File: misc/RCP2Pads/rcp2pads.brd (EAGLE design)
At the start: 16.2 x 24.1 mm, 57 parts

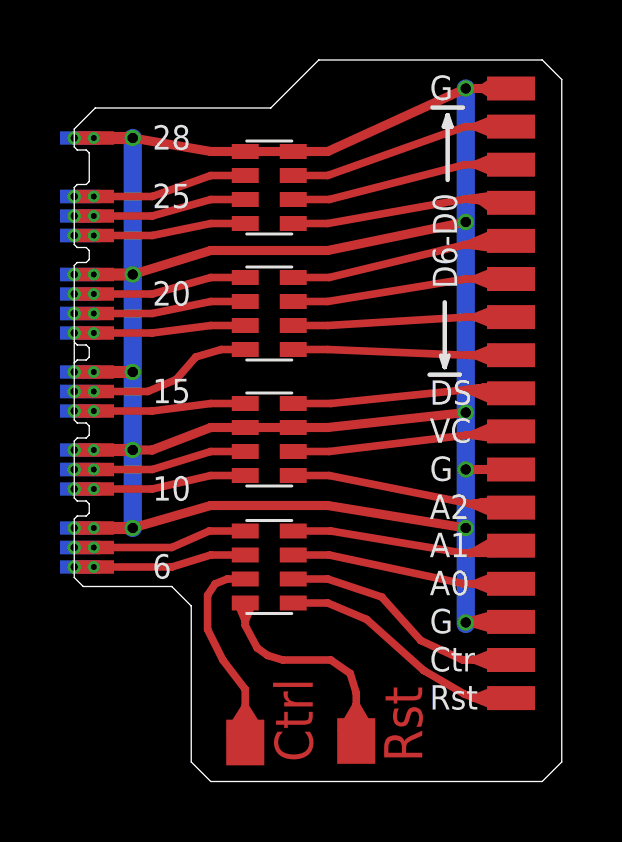
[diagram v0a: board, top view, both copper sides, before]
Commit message: upload new design for RCP2Pads
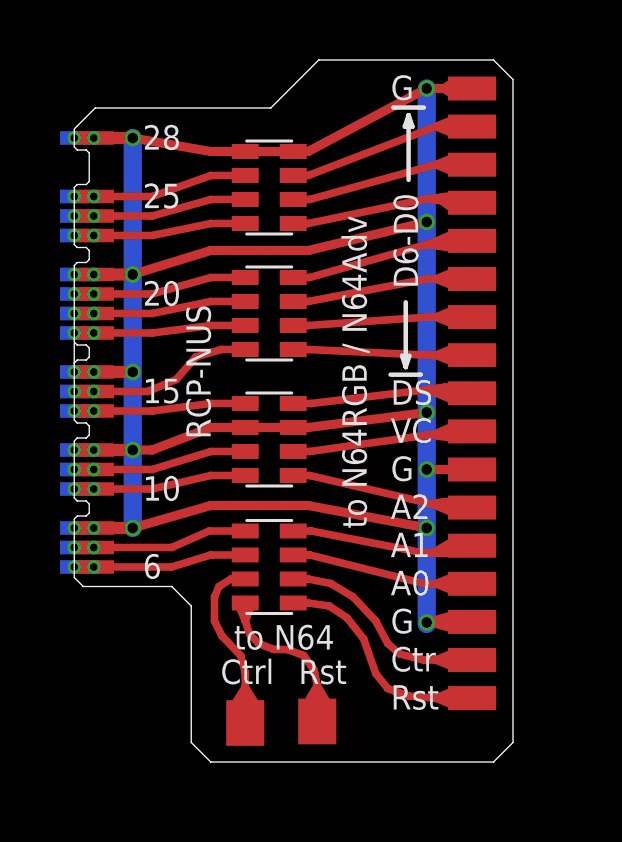
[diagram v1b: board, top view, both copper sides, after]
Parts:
- moved E$6 1.45 mm to (8.10, -8.40)
- moved E$20 1.30 mm to (13.3, 11.4)
- moved E$21 1.30 mm to (13.3, 12.7)
- moved E$36 1.30 mm to (13.3, 10.2)
- moved E$39 1.30 mm to (13.3, 8.89)
- moved E$48 1.30 mm to (13.3, 7.62)
- moved E$49 1.30 mm to (13.3, 6.35)
- moved E$50 1.30 mm to (13.3, 5.08)
- moved E$51 1.30 mm to (13.3, 3.81)
- moved E$53 1.30 mm to (13.3, 2.54)
- moved E$54 1.30 mm to (13.3, 1.27)
- moved E$55 1.30 mm to (13.3, 0.00)
- moved E$56 1.30 mm to (13.3, -1.27)
- moved E$57 1.30 mm to (13.3, -2.54)
- moved E$58 1.30 mm to (13.3, -3.81)
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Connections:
- new net S$2: E$12.P$1, E$29.P$1
- net GND: no longer E$12.P$1, E$29.P$1
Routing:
- net GND: track 92.5 -> 86.1 mm, vias 21 -> 18
- net RST: track 10.5 -> 8.66 mm
- net S$2: track 0.00 -> 1.30 mm, vias 0 -> 3
- net D6.1: track 9.63 -> 8.33 mm
- net D5.1: track 9.14 -> 7.85 mm
- net #DSYNC.1: track 10.0 -> 8.74 mm
- net VCLK.1: track 9.86 -> 8.57 mm
- net D4.1: track 9.20 -> 7.91 mm
- net SDATA.1: track 9.94 -> 8.65 mm
- net D1.1: track 10.4 -> 9.13 mm
- net D2.1: track 10.8 -> 9.47 mm
- net LRCLK.1: track 10.2 -> 8.88 mm
- net SCLK.1: track 9.24 -> 7.95 mm
- net D3.1: track 9.83 -> 8.55 mm
- net D0.1: track 10.6 -> 9.29 mm
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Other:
- board size 16.2 x 24.1 mm -> 14.6 x 23.4 mm
- board text added: "RCP-NUS"
- board text added: "borti4938 __/)__/)_"
- board text added: "to N64"
- board text added: "to N64RGB / N64Adv"

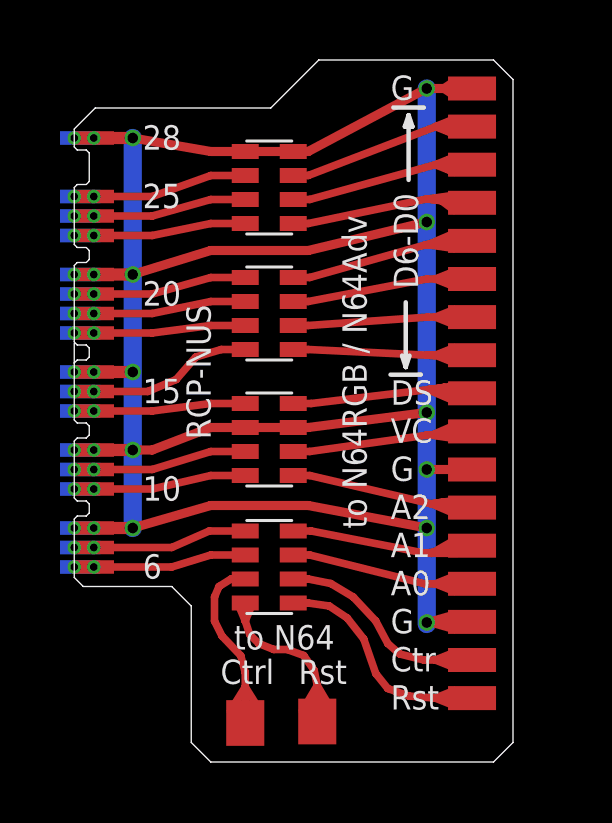
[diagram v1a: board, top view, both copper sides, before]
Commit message: update on adapter flex to include a vlck buffer
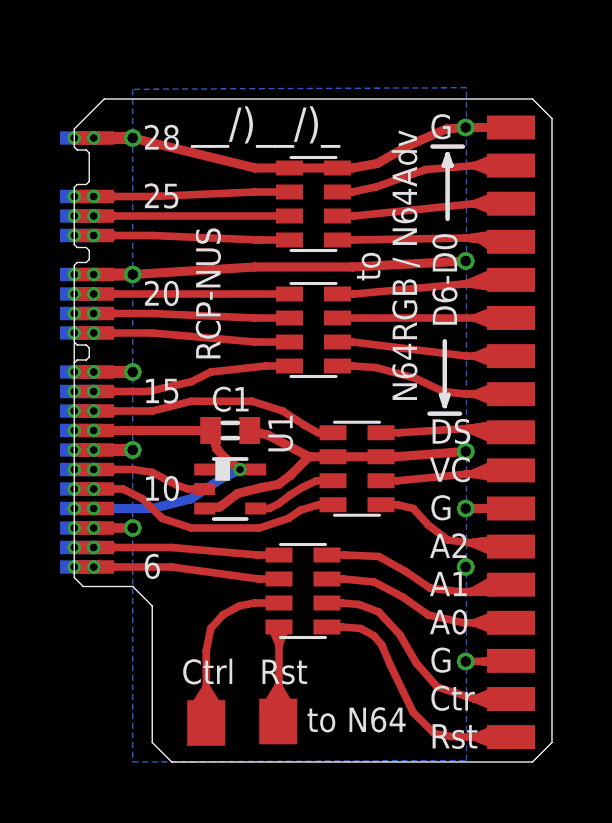
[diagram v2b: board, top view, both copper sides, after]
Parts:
- removed E$1, E$3, E$4, E$5: (no value), resistor-net:CTS742C083
- added C1: (no value), rcl:C0402
- added E$34, E$35, E$37, E$7: (no value), wirepad:SMD0,45-1,35
- added RN1, RN2, RN3, RN4: CAY16-330J4LF, resistor-net:CTS742C083
- added U1: SN74LVC1G17DCKR, 74xx-little-de:DCK_R-PDSO-G5
- moved E$36 1.84 mm to (14.6, 8.86)
- moved E$39 1.84 mm to (14.6, 7.59)
- moved E$60 1.84 mm to (14.6, -7.65)
- moved E$50 1.84 mm to (14.6, 3.78)
- moved E$51 1.84 mm to (14.6, 2.51)
- moved E$58 1.84 mm to (14.6, -5.11)
- moved E$53 1.84 mm to (14.6, 1.24)
- moved E$54 1.84 mm to (14.6, -0.03)
- moved E$55 1.84 mm to (14.6, -1.30)
- moved E$48 1.84 mm to (14.6, 6.32)
- moved E$49 1.84 mm to (14.6, 5.05)
- moved E$56 1.84 mm to (14.6, -2.57)
- moved E$57 1.84 mm to (14.6, -3.84)
- moved E$59 1.84 mm to (14.6, -6.38)
- moved E$61 1.84 mm to (14.6, -8.92)
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- renumbered E$42 to LRCLK
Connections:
- removed net S$2: E$12.P$1, E$29.P$1
- new net VCC: C1.1, E$34.P$1, E$35.P$1, E$37.P$1, E$7.P$1, U1.5
- new net VCLK_BUF: RN3.3, U1.4
- net #DSYNC: now also RN3.1; no longer E$5.1
- net #DSYNC.1: now also E$53.1, RN3.8; no longer E$5.8, E$53.P$1
- net CTRL: now also RN4.7; no longer E$1.7
- net CTRL.1: now also E$60.1, RN4.2; no longer E$1.2, E$60.P$1
- net D0: now also RN1.2; no longer E$3.2
- net D0.1: now also E$20.1, RN1.7; no longer E$20.P$1, E$3.7
- net D1: now also RN1.3; no longer E$3.3
- net D1.1: now also E$36.1, RN1.6; no longer E$3.6, E$36.P$1
- net D2: now also RN1.4; no longer E$3.4
- net D2.1: now also E$39.1, RN1.5; no longer E$3.5, E$39.P$1
- net D3: now also RN2.1; no longer E$4.1
- net D3.1: now also E$48.1, RN2.8; no longer E$4.8, E$48.P$1
- net D4: now also RN2.2; no longer E$4.2
- net D4.1: now also E$49.1, RN2.7; no longer E$4.7, E$49.P$1
- net D5: now also RN2.3; no longer E$4.3
- net D5.1: now also E$50.1, RN2.6; no longer E$4.6, E$50.P$1
- net D6: now also RN2.4; no longer E$4.4
- net D6.1: now also E$51.1, RN2.5; no longer E$4.5, E$51.P$1
- net GND: now also C1.2, E$12.P$1, E$21.1, E$29.P$1, E$55.1, E$59.1, RN1.1, RN1.8, RN3.2, RN3.7, U1.3; no longer E$21.P$1, E$3.1, E$3.8, E$5.2, E$5.7, E$55.P$1, E$59.P$1
- net LRCLK: now also RN3.4; no longer E$5.4
- net LRCLK.1: now also E$56.1, RN3.5; no longer E$5.5, E$56.P$1
- net RST: now also RN4.8; no longer E$1.8
- net RST.1: now also E$61.1, RN4.1; no longer E$1.1, E$61.P$1
- net SCLK: now also RN4.6; no longer E$1.6
- net SCLK.1: now also E$58.1, RN4.3; no longer E$1.3, E$58.P$1
- net SDATA: now also RN4.5; no longer E$1.5
- net SDATA.1: now also E$57.1, RN4.4; no longer E$1.4, E$57.P$1
- net VCLK: now also U1.2; no longer E$5.3
- net VCLK.1: now also E$54.1, RN3.6; no longer E$5.6, E$54.P$1
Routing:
- net GND: track 86.1 -> 54.7 mm, vias 18 -> 21
- net VCC: track 0.00 -> 12.8 mm, vias 0 -> 5
- net #DSYNC: track 5.07 -> 9.37 mm, vias 1 -> 2
- net LRCLK: track 5.10 -> 9.19 mm, vias 0 -> 2
- net VCLK_BUF: track 0.00 -> 2.83 mm
- net D2: track 5.09 -> 7.78 mm, vias 1 -> 2
- net D5: track 5.07 -> 7.64 mm, vias 1 -> 2
- net D4: track 5.09 -> 7.63 mm, vias 1 -> 2
- net D3: track 5.13 -> 7.62 mm, vias 1 -> 2
- net D1: track 5.13 -> 7.62 mm, vias 1 -> 2
- net D0: track 5.17 -> 7.63 mm, vias 1 -> 2
- net D6: track 5.51 -> 7.75 mm, vias 1 -> 2
- net RST: track 8.66 -> 6.43 mm
- net SCLK: track 5.11 -> 6.85 mm, vias 0 -> 2
- net #DSYNC.1: track 8.74 -> 7.05 mm
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- added copper zone on layer 16, net GND
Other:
- board size 14.6 x 23.4 mm -> 15.9 x 22.1 mm
- board text added: "__/)__/)_"

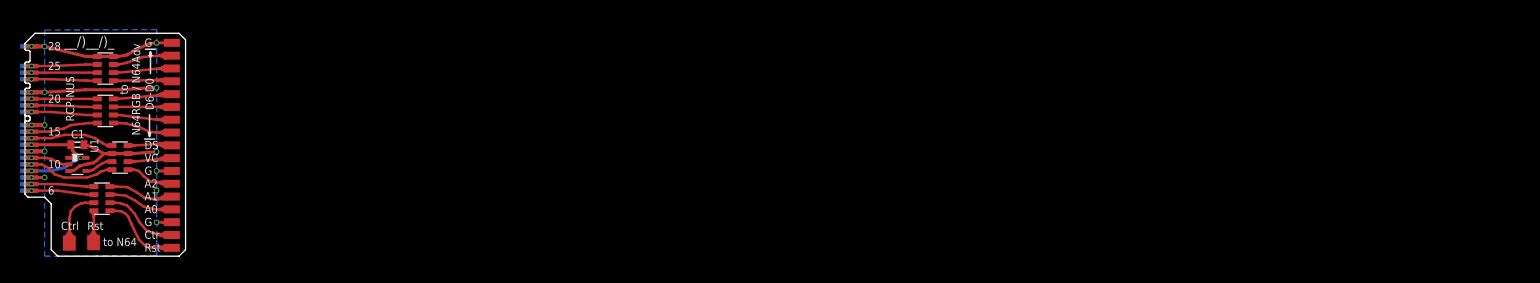
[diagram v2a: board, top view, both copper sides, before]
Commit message: update flex PCBs with suitable buffering
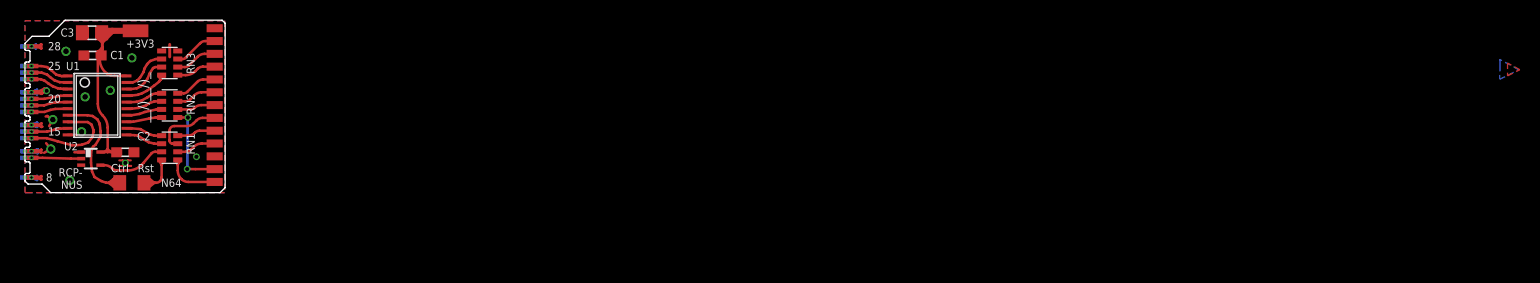
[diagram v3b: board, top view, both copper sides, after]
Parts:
- removed E$34, E$35, E$37, E$38, E$40, E$41, E$44, E$45, E$7, LRCLK: (no value), wirepad:SMD0,45-1,35
- removed E$58, E$59, E$60, E$61: (no value), wirepad:SMD0,8-1,6
- removed RN4: CAY16-330J4LF, resistor-net:CTS742C083
- added C2: 0.1u, rcl:C0603
- added C3: 22u, rcl:C0805
- added P_VCC_3V3: (no value), wirepad@1:SMD1,27-2,54
- added U2: SN74LVC1G17DCKR, texas:DCK_R-PDSO-G5
- C1: value (none) -> 0.1u; device rcl:C0402 -> rcl:C0603
- RN1, RN2, RN3: value CAY16-330J4LF -> (none)
- U1: value SN74LVC1G17DCKR -> 74VHC9151FT; device 74xx-little-de:DCK_R-PDSO-G5 -> sipex:TSSOP20
- moved RN3 10.6 mm to (14.3, 9.40)
- moved RN1 10.1 mm to (14.3, 1.00)
- moved C1 8.98 mm to (6.70, 10.2), turned to 180 degrees
- moved E$2 7.79 mm to (9.40, -2.48)
- moved E$6 7.75 mm to (11.8, -2.48)
- moved RN2 6.40 mm to (14.3, 5.20)
- moved U1 6.17 mm to (7.15, 5.20)
- moved E$36 4.49 mm to (18.8, 10.3)
- moved E$49 4.49 mm to (18.8, 6.50)
- moved E$50 4.49 mm to (18.8, 5.23)
- moved E$51 4.49 mm to (18.8, 3.96)
- moved E$53 4.49 mm to (18.8, 2.69)
- moved E$54 4.49 mm to (18.8, 1.42)
- moved E$55 4.49 mm to (18.8, 0.15)
- moved E$56 4.49 mm to (18.8, -1.12)
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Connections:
- removed net LRCLK: E$38.P$1, RN3.4
- removed net LRCLK.1: E$56.1, RN3.5
- removed net SCLK: E$41.P$1, RN4.6
- removed net SCLK.1: E$58.1, RN4.3
- removed net SDATA: E$40.P$1, RN4.5
- removed net SDATA.1: E$57.1, RN4.4
- removed net VCC: C1.1, E$34.P$1, E$35.P$1, E$37.P$1, E$7.P$1, U1.5
- removed net VCLK_BUF: RN3.3, U1.4
- new net 3V3: C1.1, C2.1, C3.1, P_VCC_3V3.1, U1.20, U2.5
- new net S$1: RN3.2, U1.19
- new net S$10: RN2.4, U1.13
- new net S$11: RN1.3, U2.4
- new net S$12: RN1.2, U1.11
- new net S$2: RN3.3, U1.18
- new net S$3: RN3.4, U1.17
- new net S$4: RN2.1, U1.16
- new net S$6: RN2.2, U1.15
- new net S$7: RN2.3, U1.14
- new net S$9: RN1.1, U1.12
- net #DSYNC: now also U1.8; no longer RN3.1
- net #DSYNC.1: now also RN1.8; no longer RN3.8
- net CTRL: now also U1.7; no longer RN4.7
- net CTRL.1: now also E$56.1, RN2.5; no longer E$60.1, RN4.2
- net D0: now also U1.1; no longer RN1.2
- net D0.1: now also RN3.7; no longer RN1.7
- net D1: now also U1.2; no longer RN1.3
- net D1.1: now also RN3.6; no longer RN1.6
- net D2: now also U1.3; no longer RN1.4
- net D2.1: now also RN3.5; no longer RN1.5
- net D3: now also U1.4; no longer RN2.1
- net D4: now also U1.5; no longer RN2.2
- net D5: now also U1.6; no longer RN2.3
- net D6: now also U1.9; no longer RN2.4
- net D6.1: now also RN1.7; no longer RN2.5
- net GND: now also C2.2, C3.2, RN3.1, RN3.8, U1.10, U2.3; no longer E$59.1, RN1.1, RN1.8, RN3.2, RN3.7, U1.3
- net RST: now also RN1.4; no longer RN4.8
- net RST.1: now also E$57.1, RN1.5; no longer E$61.1, RN4.1
- net VCLK: now also U2.2; no longer U1.2
- net VCLK.1: now also RN1.6; no longer RN3.6
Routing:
- net GND: track 54.7 -> 27.2 mm
- net 3V3: track 0.00 -> 26.4 mm
- net VCC: track 12.8 -> 0.00 mm, vias 5 -> 0
- net LRCLK: track 9.19 -> 0.00 mm, vias 2 -> 0
- net SDATA.1: track 9.06 -> 0.00 mm
- net SCLK.1: track 8.36 -> 0.00 mm
- net LRCLK.1: track 7.58 -> 0.00 mm
- net CTRL: track 7.62 -> 14.6 mm
- net SCLK: track 6.85 -> 0.00 mm, vias 2 -> 0
- net S$11: track 0.00 -> 6.85 mm
- net SDATA: track 6.84 -> 0.00 mm, vias 2 -> 0
- net S$3: track 0.00 -> 5.74 mm
- net D2.1: track 9.26 -> 3.88 mm
- net D1.1: track 8.82 -> 4.10 mm
- net S$1: track 0.00 -> 4.63 mm
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- added copper zone on layer 1, net GND
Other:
- board size 15.9 x 22.1 mm -> 19.9 x 17.1 mm
- board text added: "+3V3"
- board text added: "8"
- board text added: "N64"
- board text added: "RCP- NUS"
- board text added: "RCP2Pads v20200705"
- board text added: "RN1"
- board text added: "RN2"
- board text added: "RN3"
- board text removed: "10"
- board text removed: "6"
- board text removed: "A0"
- board text removed: "A1"
- board text removed: "A2"
- board text removed: "Ctr"
- board text removed: "D6-D0"
- board text removed: "DS"
- board text removed: "G"
- board text removed: "RCP-NUS"
- board text removed: "VC"
- board text removed: "borti4938 __/)__/)_"
- board text removed: "to N64"
- board text removed: "to N64RGB / N64Adv"
